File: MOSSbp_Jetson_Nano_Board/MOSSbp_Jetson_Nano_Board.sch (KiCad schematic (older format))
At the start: 42 parts, among them J1 24V, J2 Circulation Fan, J3 CO2, J4 Water Pump PWM, J5 Vent Fan, J6 Water Pump, J7 I2C, J8 Jetson_Nano_Dev, Q1 Q_NMOS_DGS, Q2 Q_NMOS_DGS, Q3 BSS138, Q4 Q_NMOS_DGS, U1 MIC4416, U2 MIC4416, U3 LMR14020, U4 PTN78020WAH, U5 MIC4416

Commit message: Added footprint associations
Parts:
- added D1, D2, D4: D, symbol Device:D
- D3: renamed from D1; footprint (none) -> Diode_SMD:D_SOD-128
- J4: footprint (none) -> Connector_JST:JST_GH_BM02B-GHS-TBT_1x02-1MP_P1.25mm_Vertical; Digi-Key_PN (none) -> 455-1578-1-ND
- J6: footprint (none) -> Connector_JST:JST_XH_B2B-XH-AM_1x02_P2.50mm_Vertical; Digi-Key_PN (none) -> 455-2247-ND
- J7: Digi-Key_PN (none) -> 455-1580-1-ND
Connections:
- net +12V: now also D1.1 (K), D2.1 (K), D4.1 (K)
- net at J2.2 (Pin_2), Q1.1 (D): now also D1.2 (A)
- net at J5.2 (Pin_2), Q4.1 (D): now also D4.2 (A)
- net at J3.2 (Pin_2), Q2.1 (D): now also D2.2 (A)
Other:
- moved on the sheet: J6
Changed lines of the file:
@@
 F 1 "24V" H 700 1200 50  0000 C CNN
 F 2 "TerminalBlock_Phoenix:TerminalBlock_Phoenix_MKDS-1,5-2_1x02_P5.00mm_Horizontal" H 700 1050 50  0001 C CNN
-F 3 "~" H 700 1050 50  0001 C CNN
+F 3 "https://media.digikey.com/pdf/Data%20Sheets/Phoenix%20Contact%20PDFs/1935161.pdf" H 700 1050 50  0001 C CNN
 F 4 "277-1667-ND" H 700 1050 50  0001 C CNN "Digi-Key_PN"
 	1    700  1050
@@
 NoConn ~ 9900 3200
 $Comp
-L power:+3.3V #PWR037
+L power:+3.3V #PWR039
 U 1 1 5E099D1C
 P 8450 1250
-F 0 "#PWR037" H 8450 1100 50  0001 C CNN
+F 0 "#PWR039" H 8450 1100 50  0001 C CNN
 F 1 "+3.3V" H 8465 1423 50  0000 C CNN
 F 2 "" H 8450 1250 50  0001 C CNN
@@
 $EndComp
 $Comp
-L power:GND #PWR038
+L power:GND #PWR040
 U 1 1 5E09ABE2
 P 8450 3250
-F 0 "#PWR038" H 8450 3000 50  0001 C CNN
+F 0 "#PWR040" H 8450 3000 50  0001 C CNN
 F 1 "GND" H 8455 3077 50  0000 C CNN
 F 2 "" H 8450 3250 50  0001 C CNN
@@
 	8450 1700 8450 2500
 $Comp
-L power:+3.3V #PWR036
+L power:+3.3V #PWR038
 U 1 1 5E09C0FA
 P 8300 2050
-F 0 "#PWR036" H 8300 1900 50  0001 C CNN
+F 0 "#PWR038" H 8300 1900 50  0001 C CNN
 F 1 "+3.3V" H 8315 2223 50  0000 C CNN
 F 2 "" H 8300 2050 50  0001 C CNN
@@
 	8300 2100 8300 2050
 $Comp
-L power:+5V #PWR039
+L power:+5V #PWR041
 U 1 1 5E09CB4C
 P 10050 1250
-F 0 "#PWR039" H 10050 1100 50  0001 C CNN
+F 0 "#PWR041" H 10050 1100 50  0001 C CNN
 F 1 "+5V" H 10065 1423 50  0000 C CNN
 F 2 "" H 10050 1250 50  0001 C CNN
@@
 Connection ~ 10050 1300
 $Comp
-L power:GND #PWR040
+L power:GND #PWR042
 U 1 1 5E09D4A8
 P 10050 3250
-F 0 "#PWR040" H 10050 3000 50  0001 C CNN
+F 0 "#PWR042" H 10050 3000 50  0001 C CNN
 F 1 "GND" H 10055 3077 50  0000 C CNN
 F 2 "" H 10050 3250 50  0001 C CNN
@@
 Power Input
 $Comp
-L Device:D_Schottky D1
+L Device:D_Schottky D3
 U 1 1 5E0C7E80
 P 3100 1950
-F 0 "D1" V 3054 2029 50  0000 L CNN
+F 0 "D3" V 3054 2029 50  0000 L CNN
 F 1 " PMEG4030EP" V 3200 1950 50  0000 L CNN
-F 2 "" H 3100 1950 50  0001 C CNN
+F 2 "Diode_SMD:D_SOD-128" H 3100 1950 50  0001 C CNN
 F 3 "~" H 3100 1950 50  0001 C CNN
 F 4 "1727-5841-1-ND" H 3100 1950 50  0001 C CNN "Digi-Key_PN"
@@
 	2850 4100 2850 4000
 Wire Wire Line
-	2850 3600 2850 3450
+	2850 3600 2850 3550
 Wire Wire Line
 	2850 3350 2850 3250
@@
 	6350 4100 6350 4000
 Wire Wire Line
-	6350 3600 6350 3450
+	6350 3600 6350 3550
 Wire Wire Line
 	6350 3350 6350 3250
@@
 	2850 5950 2850 5850
 Wire Wire Line
-	2850 5450 2850 5300
+	2850 5450 2850 5400
 Wire Wire Line
 	2850 5200 2850 5100
@@
 L Connector:Conn_01x02_Female J6
 U 1 1 5E3E542D
-P 6900 5650
-F 0 "J6" H 6928 5626 50  0000 L CNN
-F 1 "Water Pump" H 6928 5535 50  0000 L CNN
-F 2 "" H 6900 5650 50  0001 C CNN
-F 3 "~" H 6900 5650 50  0001 C CNN
-	1    6900 5650
+P 6950 5650
+F 0 "J6" H 6978 5626 50  0000 L CNN
+F 1 "Water Pump" H 6978 5535 50  0000 L CNN
+F 2 "Connector_JST:JST_XH_B2B-XH-AM_1x02_P2.50mm_Vertical" H 6950 5650 50  0001 C CNN
+F 3 "~" H 6950 5650 50  0001 C CNN
+F 4 "455-2247-ND" H 6950 5650 50  0001 C CNN "Digi-Key_PN"
+	1    6950 5650
 	1    0    0    -1
 $EndComp
@@
 L power:GND #PWR035
 U 1 1 5E3E5D52
-P 6650 5850
-F 0 "#PWR035" H 6650 5600 50  0001 C CNN
-F 1 "GND" H 6655 5677 50  0000 C CNN
-F 2 "" H 6650 5850 50  0001 C CNN
-F 3 "" H 6650 5850 50  0001 C CNN
-	1    6650 5850
-	1    0    0    -1
-$EndComp
-Wire Wire Line
-	6650 5850 6650 5750
-Wire Wire Line
-	6650 5750 6700 5750
-Wire Wire Line
-	6700 5650 6650 5650
-Wire Wire Line
-	6650 5650 6650 5550
+P 6700 5850
+F 0 "#PWR035" H 6700 5600 50  0001 C CNN
+F 1 "GND" H 6705 5677 50  0000 C CNN
+F 2 "" H 6700 5850 50  0001 C CNN
+F 3 "" H 6700 5850 50  0001 C CNN
+	1    6700 5850
+	1    0    0    -1
+$EndComp
+Wire Wire Line
+	6700 5850 6700 5750
+Wire Wire Line
+	6700 5750 6750 5750
+Wire Wire Line
+	6750 5650 6700 5650
+Wire Wire Line
+	6700 5650 6700 5550
 $Comp
 L Connector:Conn_01x02_Female J4
@@
 F 0 "J4" H 5878 5626 50  0000 L CNN
 F 1 "Water Pump PWM" H 5878 5535 50  0000 L CNN
-F 2 "" H 5850 5650 50  0001 C CNN
+F 2 "Connector_JST:JST_GH_BM02B-GHS-TBT_1x02-1MP_P1.25mm_Vertical" H 5850 5650 50  0001 C CNN
 F 3 "~" H 5850 5650 50  0001 C CNN
-F 4 "" H 5850 5650 50  0001 C CNN "Digi-Key_PN"
+F 4 "455-1578-1-ND" H 5850 5650 50  0001 C CNN "Digi-Key_PN"
 	1    5850 5650
 	1    0    0    -1
@@
 U 1 1 5E4C6106
 P 5400 5800
-F 0 "R10" H 5470 5846 50  0000 L CNN
+F 0 "R10" H 5200 5800 50  0000 L CNN
 F 1 "4.7k" V 5400 5700 50  0000 L CNN
 F 2 "" V 5330 5800 50  0001 C CNN
@@
 L power:+24V #PWR034
 U 1 1 5E2B454C
-P 6650 5550
-F 0 "#PWR034" H 6650 5400 50  0001 C CNN
-F 1 "+24V" H 6665 5723 50  0000 C CNN
-F 2 "" H 6650 5550 50  0001 C CNN
-F 3 "" H 6650 5550 50  0001 C CNN
-	1    6650 5550
+P 6700 5550
+F 0 "#PWR034" H 6700 5400 50  0001 C CNN
+F 1 "+24V" H 6715 5723 50  0000 C CNN
+F 2 "" H 6700 5550 50  0001 C CNN
+F 3 "" H 6700 5550 50  0001 C CNN
+	1    6700 5550
 	1    0    0    -1
 $EndComp
@@
 F 2 "Connector_JST:JST_GH_BM04B-GHS-TBT_1x04-1MP_P1.25mm_Vertical" H 7100 1900 50  0001 C CNN
 F 3 "~" H 7100 1900 50  0001 C CNN
+F 4 "455-1580-1-ND" H 7100 1900 50  0001 C CNN "Digi-Key_PN"
 	1    7100 1900
 	1    0    0    -1
@@
 	6800 1800 6800 1750
 $Comp
-L power:+3.3V #PWR?
+L power:+3.3V #PWR036
 U 1 1 5E3C95DF
 P 6800 1750
-F 0 "#PWR?" H 6800 1600 50  0001 C CNN
+F 0 "#PWR036" H 6800 1600 50  0001 C CNN
 F 1 "+3.3V" H 6815 1923 50  0000 C CNN
 F 2 "" H 6800 1750 50  0001 C CNN
@@
 $EndComp
 $Comp
-L power:GND #PWR?
+L power:GND #PWR037
 U 1 1 5E3CA243
 P 6800 2150
-F 0 "#PWR?" H 6800 1900 50  0001 C CNN
+F 0 "#PWR037" H 6800 1900 50  0001 C CNN
 F 1 "GND" H 6805 1977 50  0000 C CNN
 F 2 "" H 6800 2150 50  0001 C CNN
@@
 Text Notes 6600 1400 0    50   ~ 0
 I2C Interface
+$Comp
+L Device:D D1
+U 1 1 5E34FBBA
+P 2750 3400
+F 0 "D1" V 2750 3250 50  0000 L CNN
+F 1 "D" V 2850 3300 50  0000 L CNN
+F 2 "" H 2750 3400 50  0001 C CNN
+F 3 "~" H 2750 3400 50  0001 C CNN
+	1    2750 3400
+	0    1    1    0
+$EndComp
+Wire Wire Line
+	2750 3250 2850 3250
+Connection ~ 2850 3250
+Wire Wire Line
+	2750 3550 2850 3550
+Connection ~ 2850 3550
+Wire Wire Line
+	2850 3550 2850 3450
+$Comp
+L Device:D D4
+U 1 1 5E368634
+P 6250 3400
+F 0 "D4" V 6250 3250 50  0000 L CNN
+F 1 "D" V 6350 3300 50  0000 L CNN
+F 2 "" H 6250 3400 50  0001 C CNN
+F 3 "~" H 6250 3400 50  0001 C CNN
+	1    6250 3400
+	0    1    1    0
+$EndComp
+Wire Wire Line
+	6250 3550 6350 3550
+Connection ~ 6350 3550
+Wire Wire Line
+	6350 3550 6350 3450
+Wire Wire Line
+	6250 3250 6350 3250
+Connection ~ 6350 3250
+$Comp
+L Device:D D2
+U 1 1 5E37F519
+P 2750 5250
+F 0 "D2" V 2750 5100 50  0000 L CNN
+F 1 "D" V 2850 5150 50  0000 L CNN
+F 2 "" H 2750 5250 50  0001 C CNN
+F 3 "~" H 2750 5250 50  0001 C CNN
+	1    2750 5250
+	0    1    1    0
+$EndComp
+Wire Wire Line
+	2750 5100 2850 5100
+Connection ~ 2850 5100
+Wire Wire Line
+	2750 5400 2850 5400
+Connection ~ 2850 5400
+Wire Wire Line
+	2850 5400 2850 5300
 $EndSCHEMATC

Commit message: Finished assigning footprints and part numbers
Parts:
- removed Q1, Q2, Q4: Q_NMOS_DGS, Package_TO_SOT_SMD:SOT-23, symbol Device:Q_NMOS_DGS
- added Q1, Q2, Q4: DMN3404L, Package_TO_SOT_SMD:SOT-23, symbol Device:Q_NMOS_GSD
- C1, C10, C2: footprint (none) -> Capacitor_SMD:C_1206_3216Metric_Pad1.42x1.75mm_HandSolder; Digi-Key_PN (none) -> 478-11461-1-ND
- C11: footprint (none) -> Capacitor_SMD:C_0603_1608Metric_Pad1.05x0.95mm_HandSolder; Digi-Key_PN (none) -> 490-10486-1-ND
- C12, C5, C6: footprint (none) -> Capacitor_SMD:C_0603_1608Metric_Pad1.05x0.95mm_HandSolder; Digi-Key_PN (none) -> 399-7845-1-ND
- C13: footprint (none) -> Capacitor_SMD:CP_Elec_16x17.5; Digi-Key_PN (none) -> PCE3475CT-ND
- C3: value 10u -> 220u; footprint (none) -> Capacitor_SMD:CP_Elec_10x7.7; Digi-Key_PN (none) -> PCE3921CT-ND
- C4: value 4.7u -> 10u; footprint (none) -> Capacitor_SMD:C_1206_3216Metric_Pad1.42x1.75mm_HandSolder; Digi-Key_PN (none) -> 1276-6767-1-ND
- C7: footprint (none) -> Capacitor_SMD:C_0603_1608Metric_Pad1.05x0.95mm_HandSolder; Digi-Key_PN (none) -> 399-3476-1-ND
- C8: footprint (none) -> Capacitor_SMD:C_0603_1608Metric_Pad1.05x0.95mm_HandSolder; Digi-Key_PN (none) -> 311-1341-1-ND
- C9: footprint (none) -> Capacitor_SMD:C_2220_5650Metric_Pad1.97x5.40mm_HandSolder; Digi-Key_PN (none) -> 445-7935-1-ND
- D1, D2, D4: footprint (none) -> Diode_SMD:D_SMA_Handsoldering; Digi-Key_PN (none) -> 1655-1504-1-ND
- J8: symbol rg_symbols:Jetson_Nano_Dev -> MOSSbp_Jetson_Nano_Board-rescue:Jetson_Nano_Dev-rg_symbols
- L1: footprint (none) -> RG_footprints:SRR1260A-8R2Y
- R1: footprint (none) -> Resistor_SMD:R_0603_1608Metric_Pad1.05x0.95mm_HandSolder; Digi-Key_PN (none) -> P23.7KHCT-ND
- R10, R2, R3, R8: footprint (none) -> Resistor_SMD:R_0603_1608Metric_Pad1.05x0.95mm_HandSolder; Digi-Key_PN (none) -> 311-4.7KGRCT-ND
- R4: footprint (none) -> Resistor_SMD:R_0603_1608Metric_Pad1.05x0.95mm_HandSolder; Digi-Key_PN (none) -> P100KDBCT-ND
- R5: footprint (none) -> Resistor_SMD:R_0603_1608Metric_Pad1.05x0.95mm_HandSolder; Digi-Key_PN (none) -> P20065CT-ND
- R6, R7: footprint (none) -> Resistor_SMD:R_0603_1608Metric_Pad1.05x0.95mm_HandSolder; Digi-Key_PN (none) -> 311-10.0KHRCT-ND
- R9: value 732 -> 21k; footprint (none) -> Resistor_SMD:R_0603_1608Metric_Pad1.05x0.95mm_HandSolder; Digi-Key_PN (none) -> P21.0KHCT-ND
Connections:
- net GND: now also Q1.2 (S), Q2.2 (S), Q4.2 (S)
- net at D1.2 (A), J2.2 (Pin_2): now also Q1.3 (D)
- net at U1.2 (G): now also Q1.1 (G)
- net at D4.2 (A), J5.2 (Pin_2): now also Q4.3 (D)
- net at U5.2 (G): now also Q4.1 (G)
- net at D2.2 (A), J3.2 (Pin_2): now also Q2.3 (D)
- net at U2.2 (G): now also Q2.1 (G)
- no-connect marks 23 -> 24

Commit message: Started PCB design
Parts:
- C13: footprint Capacitor_SMD:CP_Elec_16x17.5 -> Capacitor_SMD:CP_Elec_8x10; Digi-Key_PN PCE3475CT-ND -> PCE3888CT-ND
- C3: footprint Capacitor_SMD:CP_Elec_10x7.7 -> Capacitor_SMD:CP_Elec_8x10.5; Digi-Key_PN PCE3921CT-ND -> PCE5025CT-ND
- D1, D2, D4: footprint Diode_SMD:D_SMA_Handsoldering -> Diode_SMD:D_SOD-123; Digi-Key_PN 1655-1504-1-ND -> MBR130T1GOSDKR-ND
- L1: footprint RG_footprints:SRR1260A-8R2Y -> RG_footprints:SRN8040-8R2Y; Digi-Key_PN SRR1260A-8R2YCT-ND -> SRN8040-8R2YCT-ND
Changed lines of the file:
@@
 encoding utf-8
 Sheet 1 1
-Title ""
-Date ""
-Rev ""
-Comp ""
+Title "MOSSbp Jetson Nano Hat"
+Date "2020-01-26"
+Rev "V0.1"
+Comp "Randipa Gunathilake"
 Comment1 ""
 Comment2 ""
@@
 F 0 "L1" V 3590 1800 50  0000 C CNN
 F 1 "8.2u" V 3499 1800 50  0000 C CNN
-F 2 "RG_footprints:SRR1260A-8R2Y" H 3400 1800 50  0001 C CNN
+F 2 "RG_footprints:SRN8040-8R2Y" H 3400 1800 50  0001 C CNN
 F 3 "~" H 3400 1800 50  0001 C CNN
-F 4 "SRR1260A-8R2YCT-ND" H 3400 1800 50  0001 C CNN "Digi-Key_PN"
+F 4 "SRN8040-8R2YCT-ND" H 3400 1800 50  0001 C CNN "Digi-Key_PN"
 	1    3400 1800
 	0    -1   -1   0
@@
 F 0 "C13" H 5868 2046 50  0000 L CNN
 F 1 "330u" H 5868 1955 50  0000 L CNN
-F 2 "Capacitor_SMD:CP_Elec_16x17.5" H 5788 1850 50  0001 C CNN
+F 2 "Capacitor_SMD:CP_Elec_8x10" H 5788 1850 50  0001 C CNN
 F 3 "~" H 5750 2000 50  0001 C CNN
-F 4 "PCE3475CT-ND" H 5750 2000 50  0001 C CNN "Digi-Key_PN"
+F 4 "PCE3888CT-ND" H 5750 2000 50  0001 C CNN "Digi-Key_PN"
 	1    5750 2000
 	1    0    0    -1
@@
 F 0 "D1" V 2750 3250 50  0000 L CNN
 F 1 "D" V 2850 3300 50  0000 L CNN
-F 2 "Diode_SMD:D_SMA_Handsoldering" H 2750 3400 50  0001 C CNN
+F 2 "Diode_SMD:D_SOD-123" H 2750 3400 50  0001 C CNN
 F 3 "~" H 2750 3400 50  0001 C CNN
-F 4 "1655-1504-1-ND" H 2750 3400 50  0001 C CNN "Digi-Key_PN"
+F 4 "MBR130T1GOSDKR-ND" H 2750 3400 50  0001 C CNN "Digi-Key_PN"
 	1    2750 3400
 	0    1    1    0
@@
 F 0 "D4" V 6250 3250 50  0000 L CNN
 F 1 "D" V 6350 3300 50  0000 L CNN
-F 2 "Diode_SMD:D_SMA_Handsoldering" H 6250 3400 50  0001 C CNN
+F 2 "Diode_SMD:D_SOD-123" H 6250 3400 50  0001 C CNN
 F 3 "~" H 6250 3400 50  0001 C CNN
-F 4 "1655-1504-1-ND" H 6250 3400 50  0001 C CNN "Digi-Key_PN"
+F 4 "MBR130T1GOSDKR-ND" H 6250 3400 50  0001 C CNN "Digi-Key_PN"
 	1    6250 3400
 	0    1    1    0
@@
 F 0 "D2" V 2750 5100 50  0000 L CNN
 F 1 "D" V 2850 5150 50  0000 L CNN
-F 2 "Diode_SMD:D_SMA_Handsoldering" H 2750 5250 50  0001 C CNN
+F 2 "Diode_SMD:D_SOD-123" H 2750 5250 50  0001 C CNN
 F 3 "~" H 2750 5250 50  0001 C CNN
-F 4 "1655-1504-1-ND" H 2750 5250 50  0001 C CNN "Digi-Key_PN"
+F 4 "MBR130T1GOSDKR-ND" H 2750 5250 50  0001 C CNN "Digi-Key_PN"
 	1    2750 5250
 	0    1    1    0
@@
 F 0 "C3" H 900 2200 50  0000 L CNN
 F 1 "220u" H 900 2000 50  0000 L CNN
-F 2 "Capacitor_SMD:CP_Elec_10x7.7" H 888 1950 50  0001 C CNN
+F 2 "Capacitor_SMD:CP_Elec_8x10.5" H 888 1950 50  0001 C CNN
 F 3 "~" H 850 2100 50  0001 C CNN
-F 4 "PCE3921CT-ND" H 850 2100 50  0001 C CNN "Digi-Key_PN"
+F 4 "PCE5025CT-ND" H 850 2100 50  0001 C CNN "Digi-Key_PN"
 	1    850  2100
 	1    0    0    -1

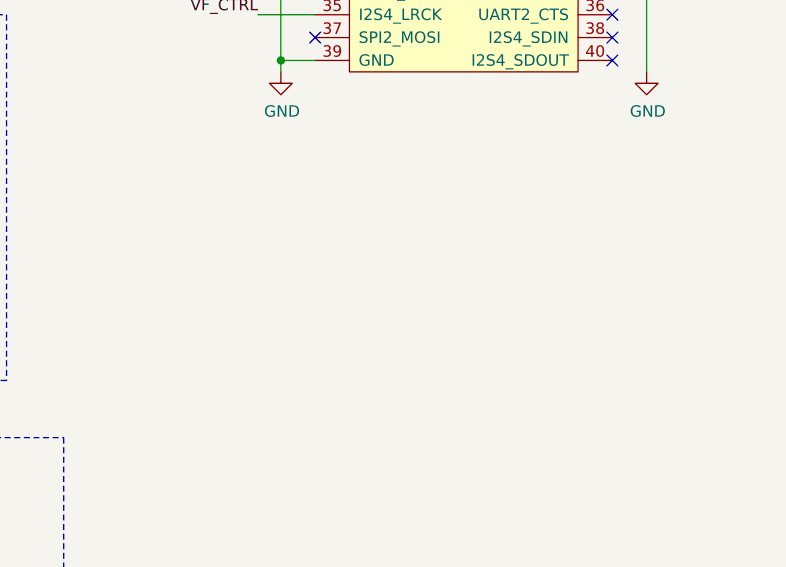
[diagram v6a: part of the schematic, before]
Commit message: Adding temperature sensors
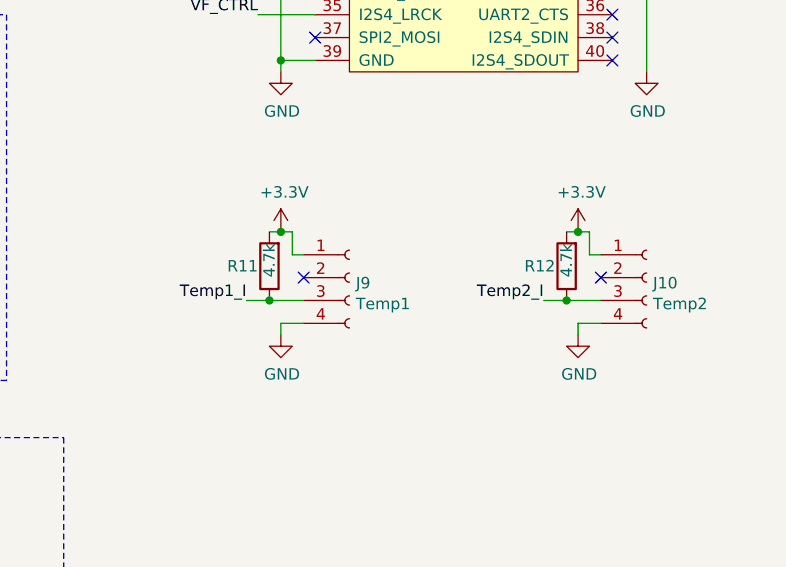
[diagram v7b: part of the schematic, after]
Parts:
- added J10: Temp2, Connector_JST:JST_GH_BM04B-GHS-TBT_1x04-1MP_P1.25mm_Vertical, symbol Connector:Conn_01x04_Female
- added J9: Temp1, Connector_JST:JST_GH_BM04B-GHS-TBT_1x04-1MP_P1.25mm_Vertical, symbol Connector:Conn_01x04_Female
- added R11, R12: 4.7k, Resistor_SMD:R_0603_1608Metric_Pad1.05x0.95mm_HandSolder, symbol Device:R
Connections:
- net +3V3: now also J10.1 (Pin_1), J9.1 (Pin_1), R11.2, R12.2
- net GND: now also J10.4 (Pin_4), J9.4 (Pin_4)
- new net Temp1_I: J9.3 (Pin_3), R11.1
- new net Temp2_I: J10.3 (Pin_3), R12.1
- no-connect marks 24 -> 26
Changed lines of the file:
@@
 	1    0    0    -1
 $EndComp
+$Comp
+L power:+3.3V #PWR045
+U 1 1 5E3028DE
+P 9750 3950
+F 0 "#PWR045" H 9750 3800 50  0001 C CNN
+F 1 "+3.3V" H 9765 4123 50  0000 C CNN
+F 2 "" H 9750 3950 50  0001 C CNN
+F 3 "" H 9750 3950 50  0001 C CNN
+	1    9750 3950
+	1    0    0    -1
+$EndComp
+$Comp
+L power:GND #PWR046
+U 1 1 5E3028E8
+P 9750 4400
+F 0 "#PWR046" H 9750 4150 50  0001 C CNN
+F 1 "GND" H 9755 4227 50  0000 C CNN
+F 2 "" H 9750 4400 50  0001 C CNN
+F 3 "" H 9750 4400 50  0001 C CNN
+	1    9750 4400
+	1    0    0    -1
+$EndComp
+Wire Wire Line
+	9850 4350 9750 4350
+Wire Wire Line
+	9750 4350 9750 4400
+$Comp
+L Connector:Conn_01x04_Female J10
+U 1 1 5E3028F9
+P 10050 4150
+F 0 "J10" H 10078 4126 50  0000 L CNN
+F 1 "Temp2" H 10078 4035 50  0000 L CNN
+F 2 "Connector_JST:JST_GH_BM04B-GHS-TBT_1x04-1MP_P1.25mm_Vertical" H 10050 4150 50  0001 C CNN
+F 3 "~" H 10050 4150 50  0001 C CNN
+F 4 "455-1580-1-ND" H 10050 4150 50  0001 C CNN "Digi-Key_PN"
+	1    10050 4150
+	1    0    0    -1
+$EndComp
+$Comp
+L Device:R R12
+U 1 1 5E32BEDB
+P 9700 4100
+F 0 "R12" H 9750 4100 50  0000 L CNN
+F 1 "4.7k" V 9700 4000 50  0000 L CNN
+F 2 "Resistor_SMD:R_0603_1608Metric_Pad1.05x0.95mm_HandSolder" V 9630 4100 50  0001 C CNN
+F 3 "~" H 9700 4100 50  0001 C CNN
+F 4 "311-4.7KGRCT-ND" H 9700 4100 50  0001 C CNN "Digi-Key_PN"
+	1    9700 4100
+	-1   0    0    1
+$EndComp
+Wire Wire Line
+	9850 4050 9800 4050
+Wire Wire Line
+	9800 4050 9800 3950
+Wire Wire Line
+	9800 3950 9750 3950
+Wire Wire Line
+	9850 4250 9700 4250
+Connection ~ 9700 4250
+Wire Wire Line
+	9700 4250 9600 4250
+Connection ~ 9750 3950
+Wire Wire Line
+	9750 3950 9700 3950
+NoConn ~ 9850 4150
+Text Label 9600 4250 2    50   ~ 0
+Temp2_I
+$Comp
+L power:+3.3V #PWR043
+U 1 1 5E3B00BB
+P 8450 3950
+F 0 "#PWR043" H 8450 3800 50  0001 C CNN
+F 1 "+3.3V" H 8465 4123 50  0000 C CNN
+F 2 "" H 8450 3950 50  0001 C CNN
+F 3 "" H 8450 3950 50  0001 C CNN
+	1    8450 3950
+	1    0    0    -1
+$EndComp
+$Comp
+L power:GND #PWR044
+U 1 1 5E3B00C5
+P 8450 4400
+F 0 "#PWR044" H 8450 4150 50  0001 C CNN
+F 1 "GND" H 8455 4227 50  0000 C CNN
+F 2 "" H 8450 4400 50  0001 C CNN
+F 3 "" H 8450 4400 50  0001 C CNN
+	1    8450 4400
+	1    0    0    -1
+$EndComp
+Wire Wire Line
+	8550 4350 8450 4350
+Wire Wire Line
+	8450 4350 8450 4400
+$Comp
+L Connector:Conn_01x04_Female J9
+U 1 1 5E3B00D2
+P 8750 4150
+F 0 "J9" H 8778 4126 50  0000 L CNN
+F 1 "Temp1" H 8778 4035 50  0000 L CNN
+F 2 "Connector_JST:JST_GH_BM04B-GHS-TBT_1x04-1MP_P1.25mm_Vertical" H 8750 4150 50  0001 C CNN
+F 3 "~" H 8750 4150 50  0001 C CNN
+F 4 "455-1580-1-ND" H 8750 4150 50  0001 C CNN "Digi-Key_PN"
+	1    8750 4150
+	1    0    0    -1
+$EndComp
+$Comp
+L Device:R R11
+U 1 1 5E3B00DD
+P 8400 4100
+F 0 "R11" H 8450 4100 50  0000 L CNN
+F 1 "4.7k" V 8400 4000 50  0000 L CNN
+F 2 "Resistor_SMD:R_0603_1608Metric_Pad1.05x0.95mm_HandSolder" V 8330 4100 50  0001 C CNN
+F 3 "~" H 8400 4100 50  0001 C CNN
+F 4 "311-4.7KGRCT-ND" H 8400 4100 50  0001 C CNN "Digi-Key_PN"
+	1    8400 4100
+	-1   0    0    1
+$EndComp
+Wire Wire Line
+	8550 4050 8500 4050
+Wire Wire Line
+	8500 4050 8500 3950
+Wire Wire Line
+	8500 3950 8450 3950
+Wire Wire Line
+	8550 4250 8400 4250
+Connection ~ 8400 4250
+Wire Wire Line
+	8400 4250 8300 4250
+Connection ~ 8450 3950
+Wire Wire Line
+	8450 3950 8400 3950
+NoConn ~ 8550 4150
+Text Label 8300 4250 2    50   ~ 0
+Temp1_I
 $EndSCHEMATC
